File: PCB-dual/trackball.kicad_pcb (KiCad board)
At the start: 2 copper layers, 48.8 x 41.5 mm, 8 parts, among them J3 Conn_01x01_Male, Q1 MMBT2222A-7-F, U1 Adafruit_QT_Py_M0, U2 MrJohnK_PMW3360DM-T2QU, U3 MrJohnK_PMW3360DM-T2QU

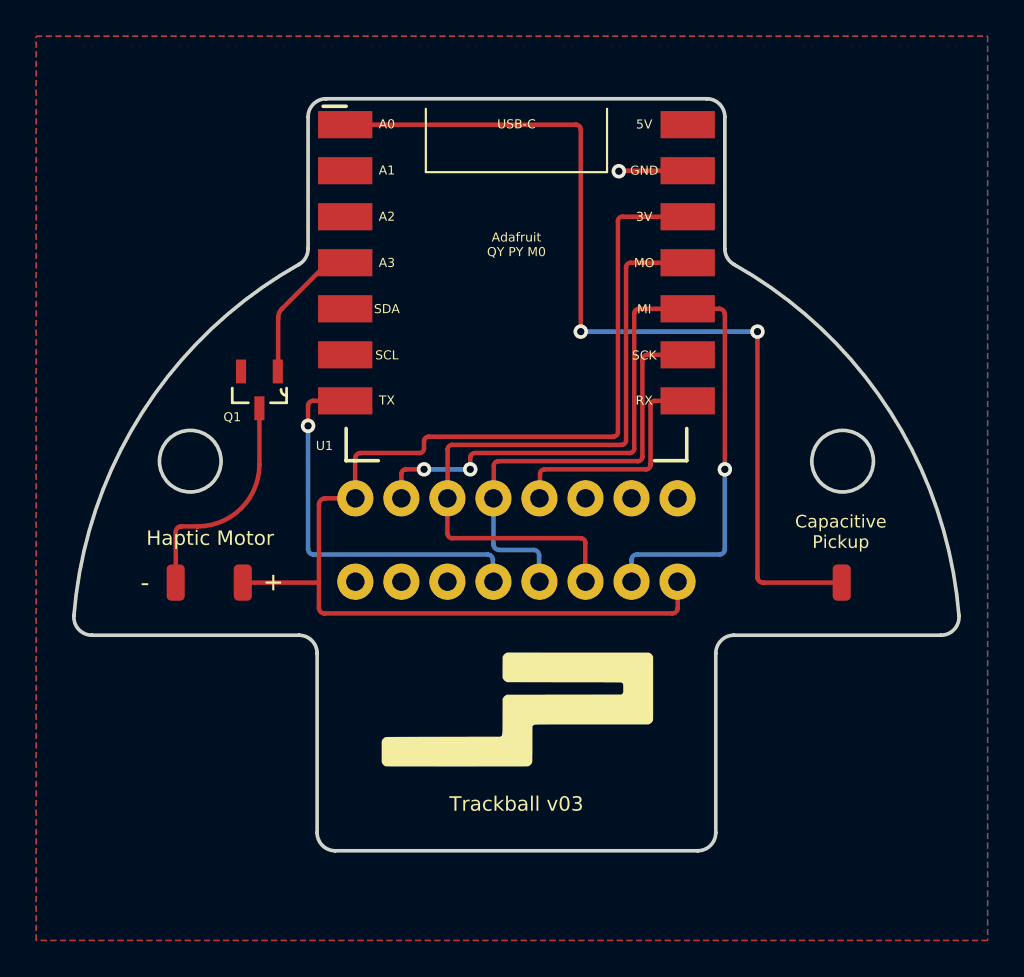
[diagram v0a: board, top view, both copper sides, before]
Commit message: feat: v1.4 with ~3.4mm spacing between sensor header pins on center with new case optimization, QTPy positioning fix, new ground pad for grounding to case, few track tweaks
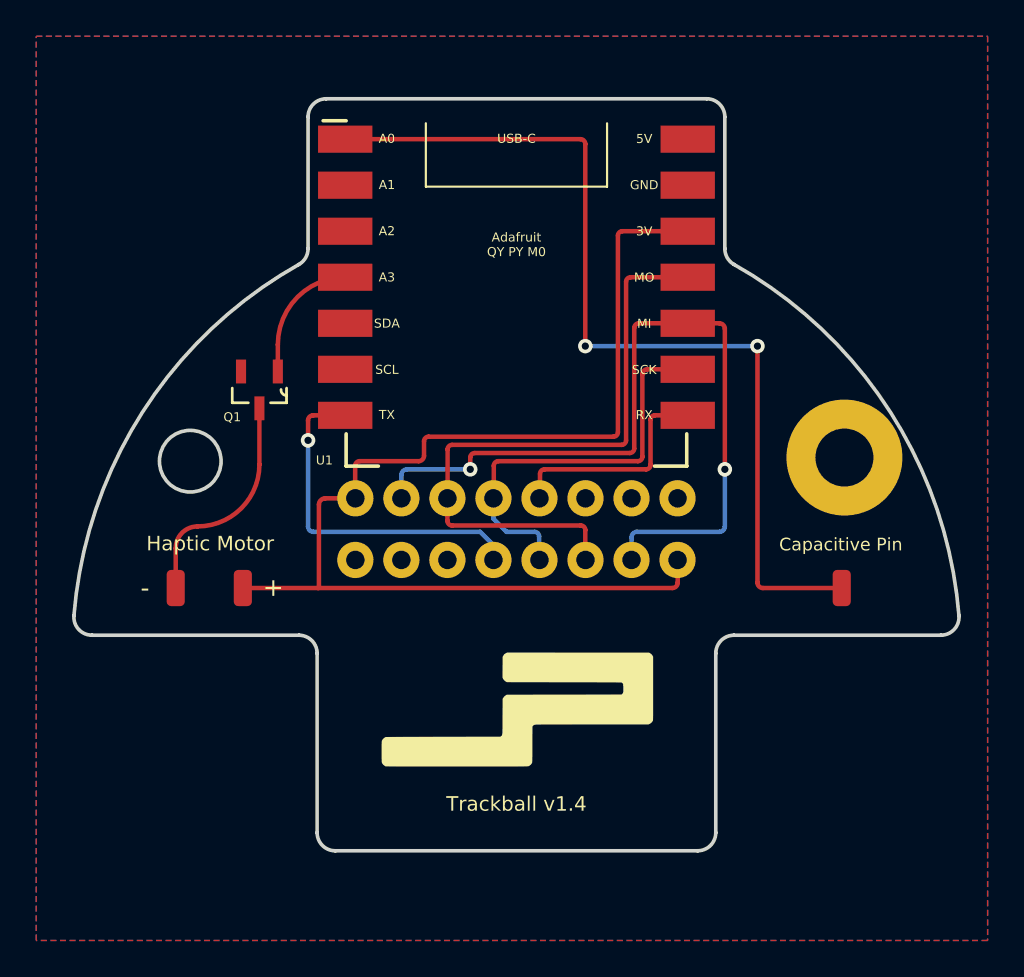
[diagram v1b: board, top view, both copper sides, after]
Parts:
- added H1: MountingHole_Pad, MountingHole:MountingHole_3.2mm_M3_Pad, F.Cu at (162.6, 141.8)
- moved U3 1.20 mm to (144.5, 156.4)
- moved U1 0.80 mm to (144.5, 131.8)
- moved + 0.30 mm to (129.4, 148.9)
- moved - 0.30 mm to (125.7, 148.9)
- moved J3 0.30 mm to (162.4, 148.9)
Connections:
- net GND renamed Net-(Q1-Pad2)
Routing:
- net Net-(Q1-Pad2): track 3.82 -> 0.00 mm, vias 1 -> 0
- net Net-(U1-Pad12): track 47.6 -> 44.8 mm, vias 3 -> 2
- net Net-(U1-Pad7): track 21.8 -> 19.6 mm
- net Net-(J1-Pad1): track 67.0 -> 64.7 mm
- net Net-(U1-Pad13): track 25.1 -> 22.9 mm
- net Net-(U1-Pad11): track 37.9 -> 35.9 mm
- net Net-(Q1-Pad1): track 8.09 -> 7.25 mm
- net Net-(U1-Pad14): track 13.2 -> 12.4 mm
- net Net-(J3-Pad1): track 52.4 -> 51.9 mm
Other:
- outline, holes or cut-outs redrawn
- board text added: "Capacitive Pin"
- board text added: "Trackball v1.4"
- board text removed: "Capacitive Pickup"
- board text removed: "Trackball v03"
